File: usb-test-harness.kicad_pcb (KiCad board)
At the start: 4 copper layers, 98 x 85 mm, 85 parts, among them J1 5V_RAW, J10 USB_A_DUAL, J2 GND, J3 V_EXT, J4 USB_A (female down), J5 Conn_01x03_Male, J6 USB_A_DUAL, J7 USB_A_DUAL, J8 USB_A SOFNG USB-05, J9 USB_B_Micro (up), U1 FT24C02A, U2 SE5120ST33, U3 USB2517, U4 APL3511C, U5 APL3511C, U6 APL3511C, U7 APL3511C, U8 APL3511C, U9 APL3511C, Y1 24MHz

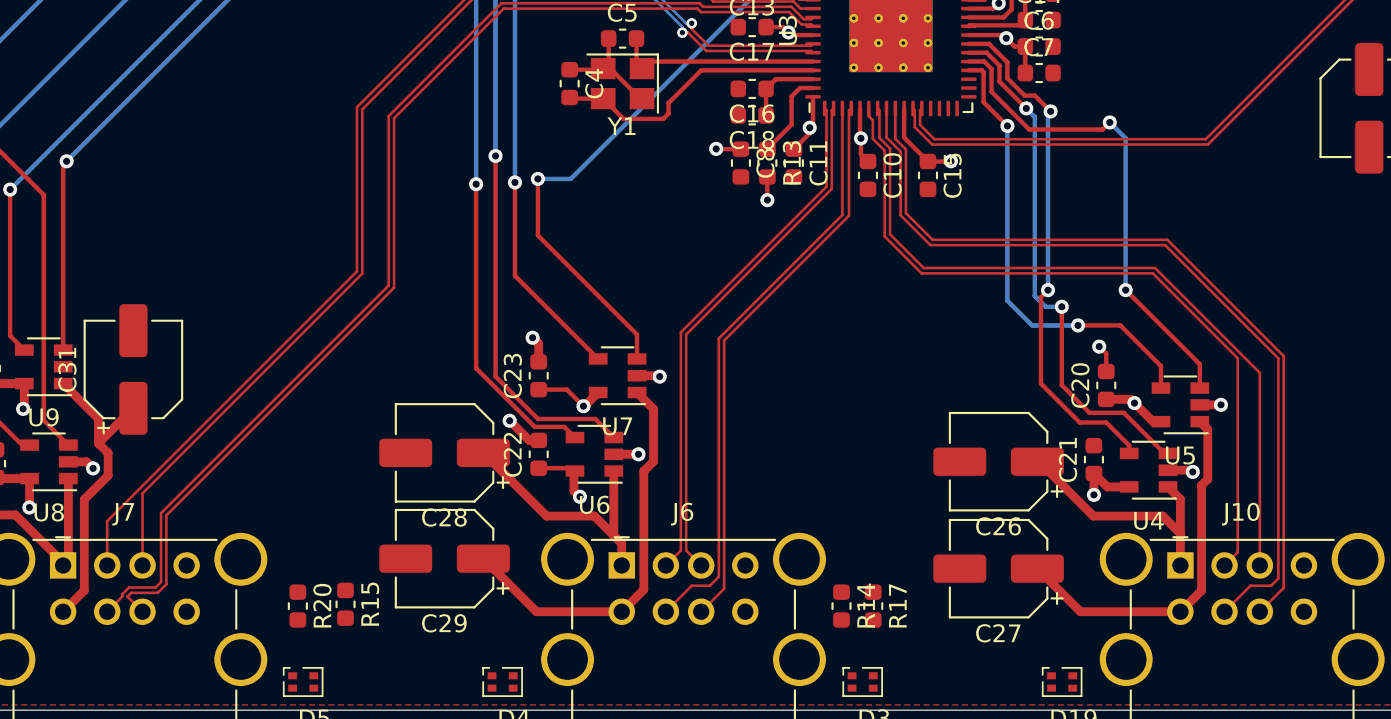
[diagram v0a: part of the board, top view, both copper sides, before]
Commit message: usb-hub: fix more diff pairs broken by moving things.
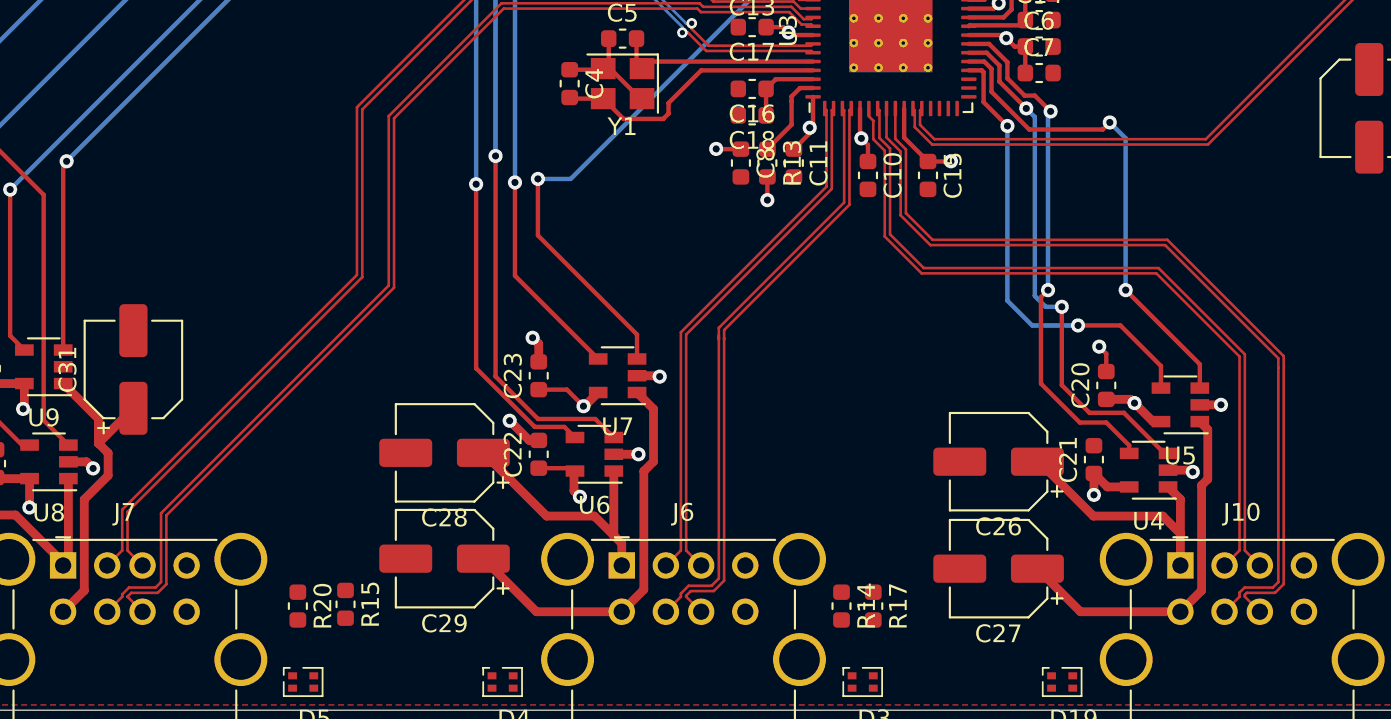
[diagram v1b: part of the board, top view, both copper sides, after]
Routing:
- net /downstream-port-power/U2+: track 46.0 -> 47.6 mm
- net /downstream-port-power/U4+: track 32.0 -> 33.6 mm
- net /downstream-port-power/U5+: track 59.8 -> 60.5 mm
- net /downstream-port-power/U4-: track 33.2 -> 33.8 mm

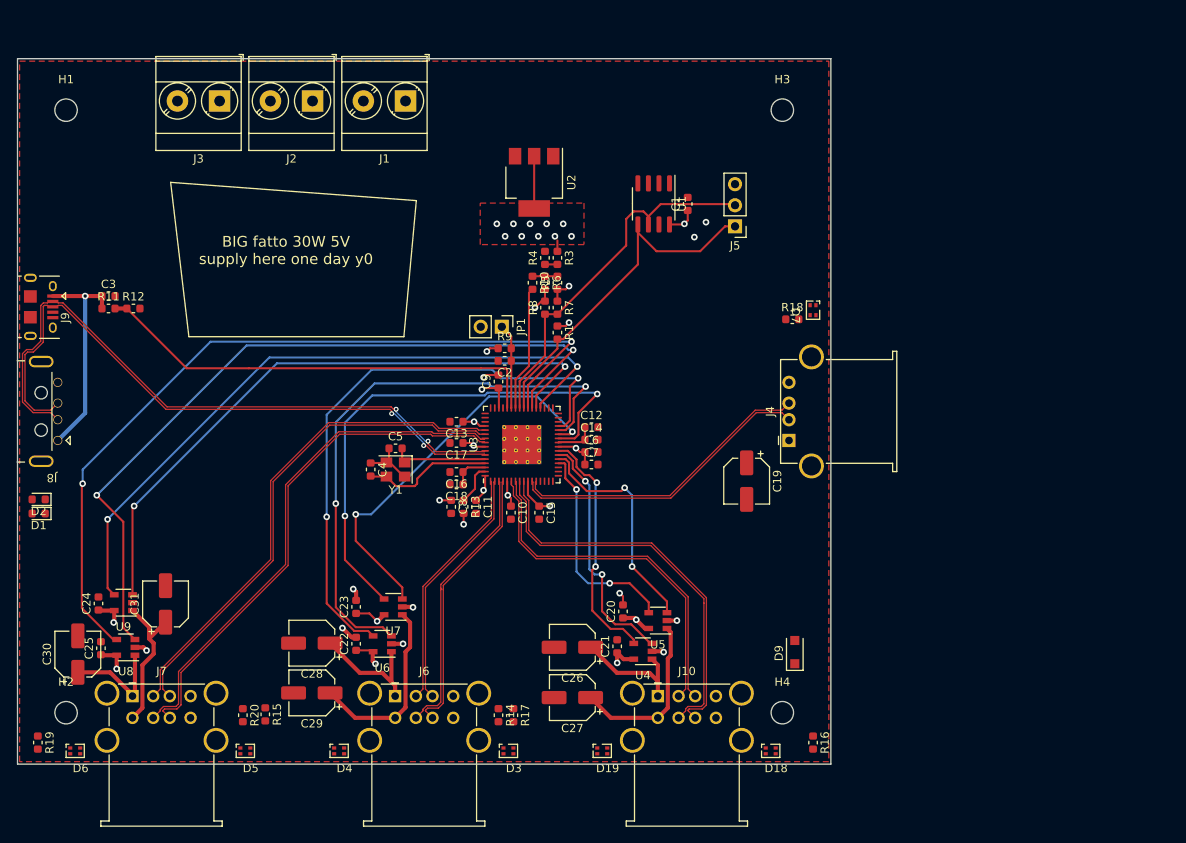
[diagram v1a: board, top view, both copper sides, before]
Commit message: usb-hub: just shields and silk left.
finished all the leds and controls
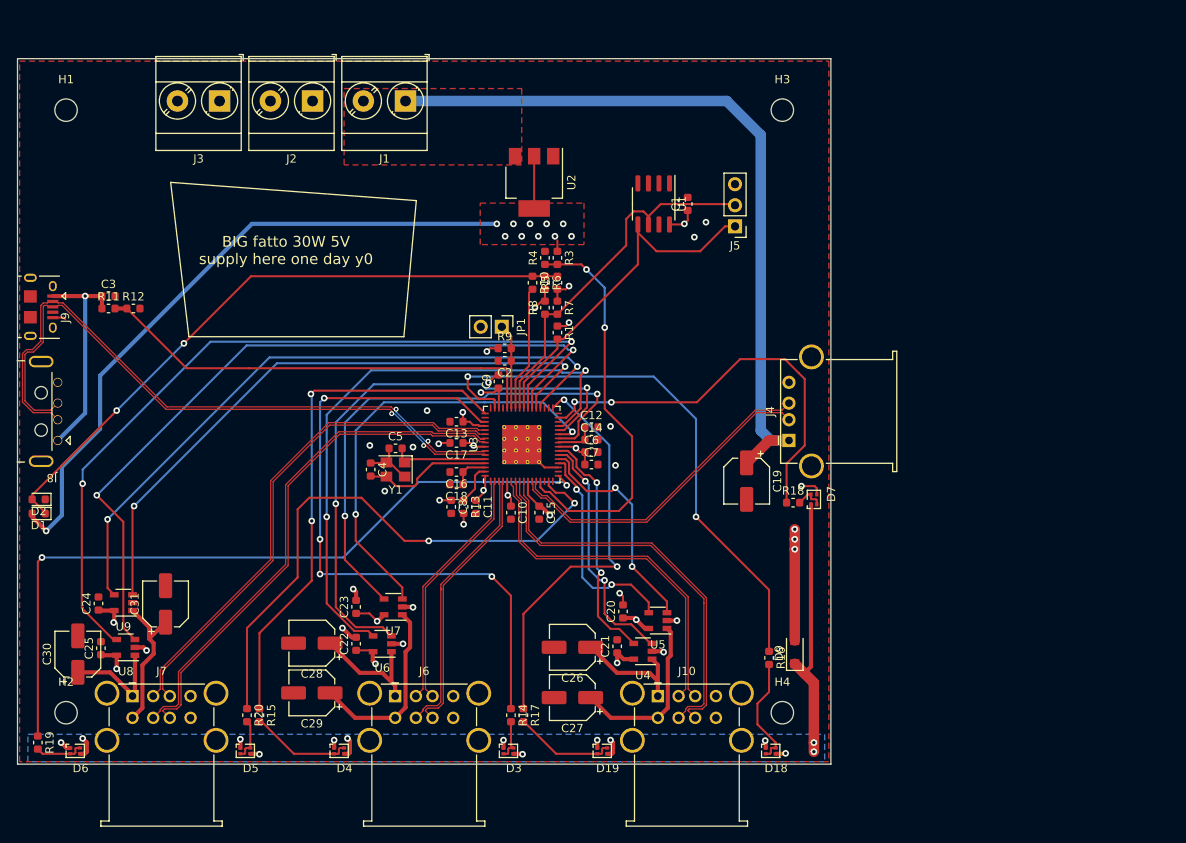
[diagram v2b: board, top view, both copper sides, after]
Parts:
- moved D7 22.8 mm to (195.2, 103.7), turned to 90 degrees
- moved R18 22.1 mm to (192.7, 104.1)
- moved R16 11.5 mm to (189.8, 122.8)
- moved R14 1.50 mm to (158.7, 129.7)
- moved R17 1.20 mm to (160.2, 129.7)
- moved R15 0.71 mm to (128.4, 129.7)
- moved R20 0.50 mm to (126.9, 129.7)
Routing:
- net +3V3: track 45.3 -> 140.2 mm, vias 22 -> 26
- net /upstream-config-leds/LED_A6: track 0.00 -> 90.4 mm, vias 0 -> 2
- net +5V: track 21.8 -> 112.0 mm
- net /upstream-config-leds/LED_A1: track 0.00 -> 79.7 mm, vias 0 -> 4
- net /upstream-config-leds/CFG_SEL1: track 3.00 -> 77.1 mm, vias 0 -> 2
- net /upstream-config-leds/LED_A7: track 0.00 -> 69.1 mm, vias 0 -> 2
- net /upstream-config-leds/LED_A3: track 0.00 -> 67.5 mm, vias 0 -> 2
- net /upstream-config-leds/LED_A2: track 0.00 -> 62.9 mm, vias 0 -> 2
- net /upstream-config-leds/LED_A5: track 0.00 -> 50.0 mm, vias 0 -> 2
- net /upstream-config-leds/LED_A4: track 0.00 -> 49.6 mm, vias 0 -> 2
- net /upstream-config-leds/CFG_SEL2: track 1.50 -> 48.7 mm, vias 0 -> 2
- net /upstream-config-leds/LED_DRIVE: track 0.00 -> 38.4 mm, vias 0 -> 8
- net GND: track 24.9 -> 44.0 mm, vias 13 -> 27
- net /upstream-config-leds/LA_3-1: track 0.00 -> 13.3 mm
- net /upstream-config-leds/LA_2-4: track 0.00 -> 12.4 mm
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- added copper zone on F.Cu, net +5V
- added copper zone on B.Cu, net /upstream-config-leds/LED_DRIVE

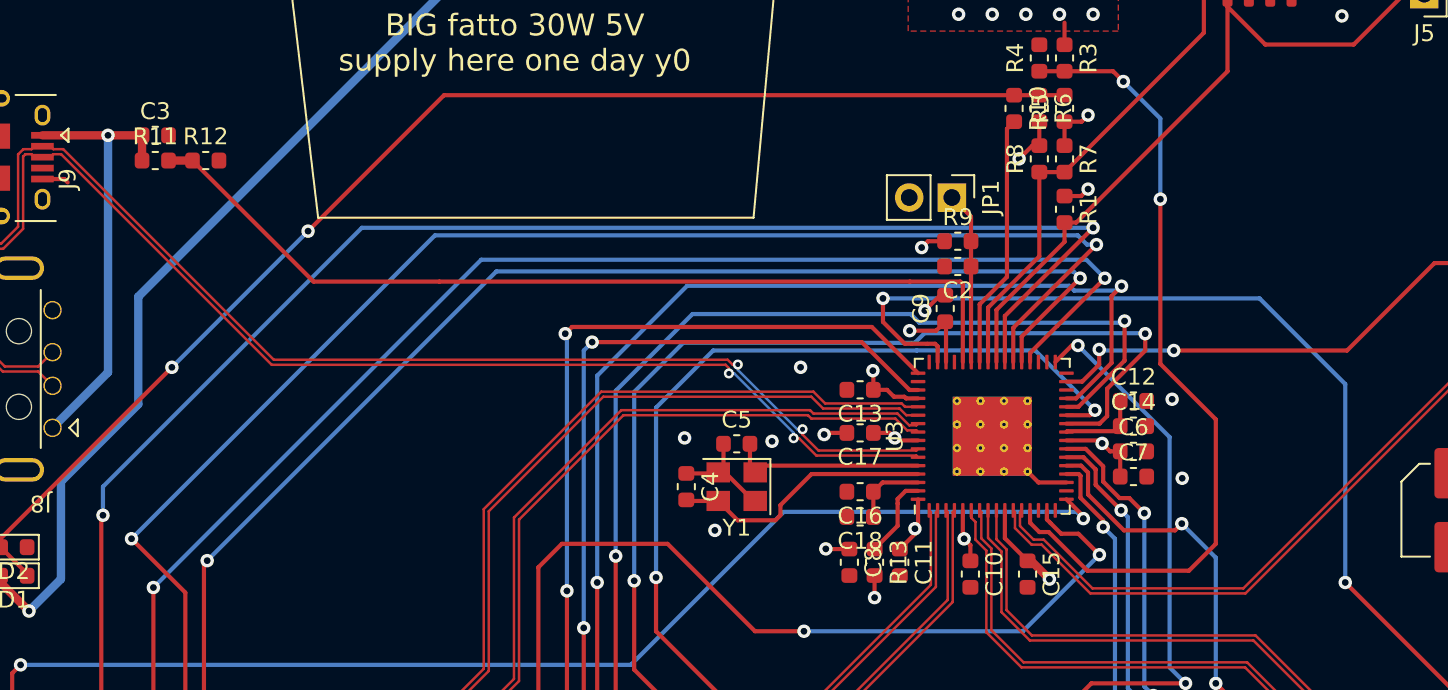
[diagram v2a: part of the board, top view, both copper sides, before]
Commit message: usb-hub: add local power connection
Somehow felt that "dynamic power" was going to magically save things
here.  It does not!  required a bit of re-routing.
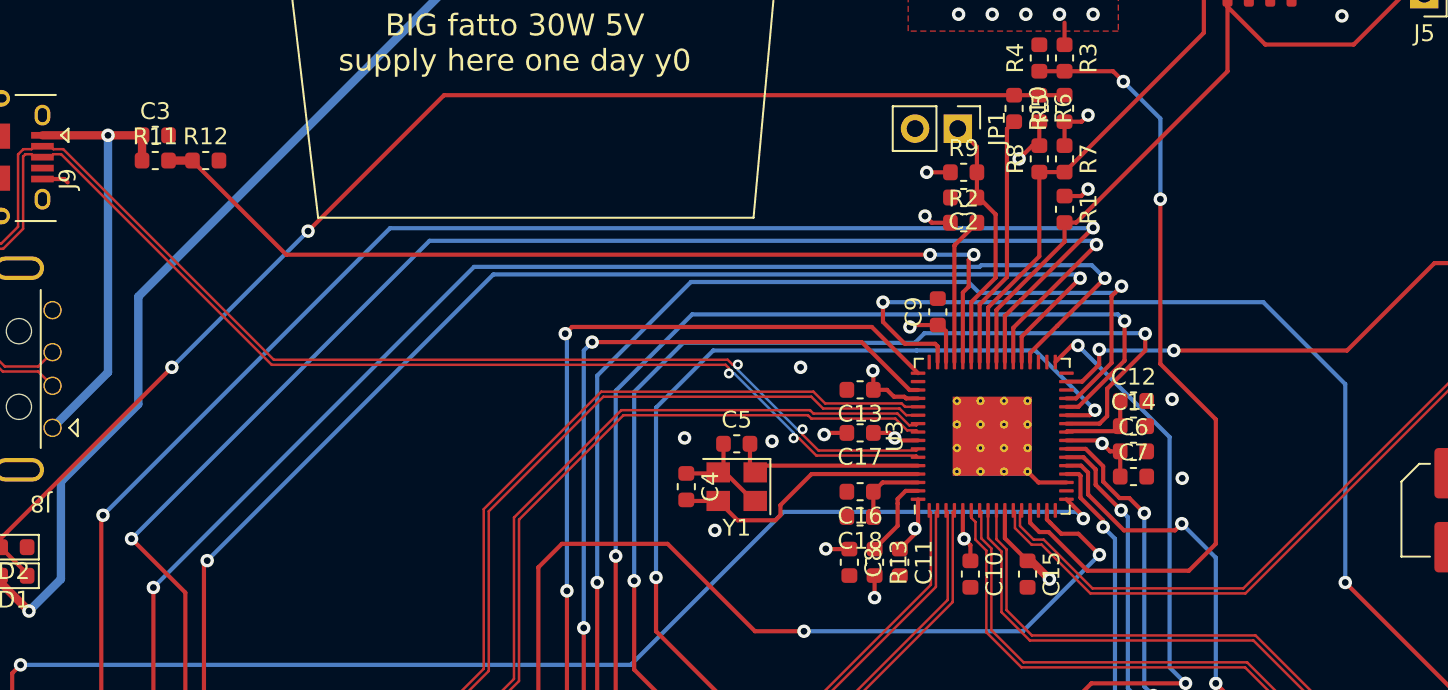
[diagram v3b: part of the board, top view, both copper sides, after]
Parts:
- added R2: 10k, Resistor_SMD:R_0603_1608Metric, F.Cu at (158.3, 84.4)
- moved JP1 4.11 mm to (157.9, 78.8)
- moved C2 4.11 mm to (158.3, 82.9)
- moved R9 4.11 mm to (158.3, 81.4)
- moved C9 0.48 mm to (156.8, 89.7)
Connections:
- U3 pad 45: (no net) -> /upstream-config-leds/LOCAL_PWR
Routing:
- net /upstream-config-leds/LOCAL_PWR: track 0.00 -> 8.85 mm
- net /upstream-config-leds/~RESET: track 10.3 -> 15.5 mm
- net /upstream-config-leds/VBUS_DET: track 54.9 -> 56.9 mm, vias 0 -> 2
- net GND: track 44.0 -> 42.4 mm, vias 27 -> 26
- net /downstream-port-power/EN5: track 97.9 -> 97.0 mm
- net +3V3: track 140.2 -> 141.1 mm, vias 26 -> 27

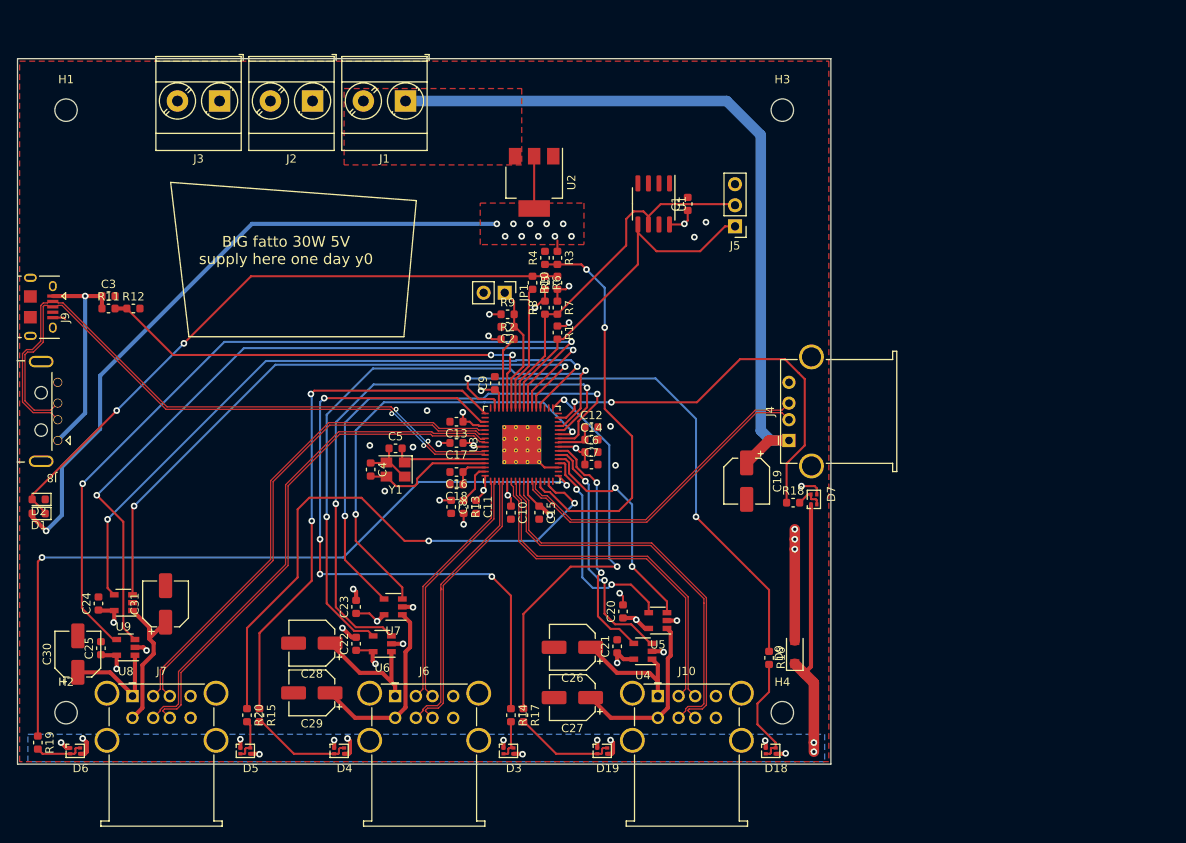
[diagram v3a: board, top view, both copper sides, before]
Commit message: usb-hub: expand spacing on top ground
cypress design guide, try not to have same plane ground too close to
d+/d- traces
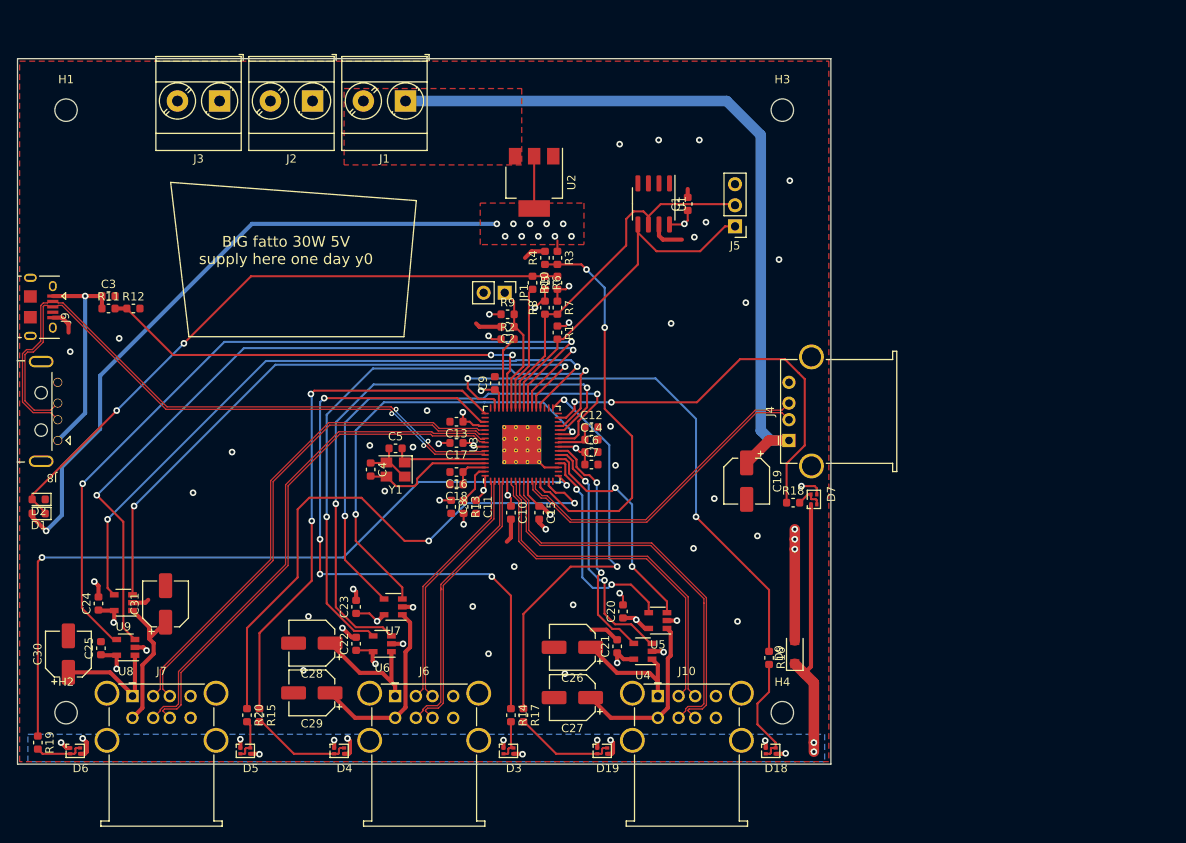
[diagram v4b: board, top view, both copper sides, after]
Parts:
- moved C30 1.14 mm to (105.4, 122.3)
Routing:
- net GND: track 42.4 -> 67.5 mm, vias 26 -> 50
- net /downstream-port-power/VBUS5: track 12.9 -> 14.0 mm

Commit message: usb-hub: decide shields per app note
SMSC 15.17 guidelines for usb hubs seem sensible and relevant.
Connect all the shields together, and to ground at one point.
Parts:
- added C32: .1uF, Capacitor_SMD:C_0603_1608Metric, F.Cu at (105.9, 72.8)
- added R21: 330, Resistor_SMD:R_0603_1608Metric, F.Cu at (105.9, 74.3)
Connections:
- J10 pad 9: Net-(J10-Pad9) -> GNDPWR
- J4 pad 5: Net-(J4-Pad5) -> GNDPWR
- J6 pad 9: Net-(J6-Pad9) -> GNDPWR
- J7 pad 9: Net-(J7-Pad9) -> GNDPWR
- J8 pad 5: Net-(J8-Pad5) -> GNDPWR
- J9 pad 6: Net-(J9-Pad6) -> GNDPWR
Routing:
- net GNDPWR: track 0.00 -> 334.6 mm
- net GND: vias 50 -> 54
- added copper zone on B.Cu, net GND
